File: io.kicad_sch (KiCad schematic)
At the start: 20 parts, among them J3 USB_C_Receptacle_USB2.0, J4 Conn_01x06_Male, U3 USBLC6-2SC6

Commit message: rev-7 ready
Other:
- note added: "USB ESD Protection"
- note removed: "ESD Protection"
- note removed: "Power Output"
- moved on the sheet: BUZZER1, C23, C24, C25, C26, J3, J4, LED1, R15, R16, R17, R18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

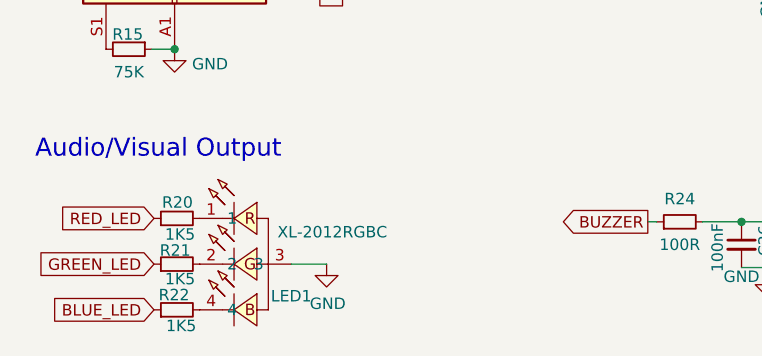
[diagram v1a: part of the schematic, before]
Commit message: fix led polarity
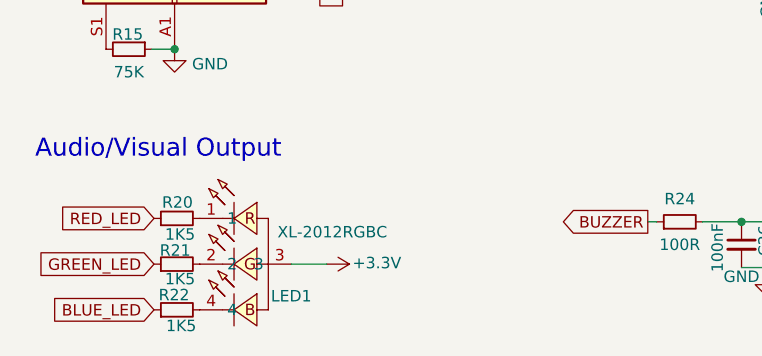
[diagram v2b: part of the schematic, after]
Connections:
- net +3.3V: now also LED1.3
- net GND: no longer LED1.3
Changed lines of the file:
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@@
     (pin "2")
-  )
-  (symbol (lib_id "power:GND") (at 44.704 79.248 0) (unit 1)
-    (in_bom yes) (on_board yes)
-    (property "Reference" "#PWR063" (id 0) (at 44.704 85.598 0)
-      (effects (font (size 1.27 1.27)) hide)
-    )
-    (property "Value" "GND" (id 1) (at 44.831 83.6422 0))
-    (property "Footprint" "" (id 2) (at 44.704 79.248 0)
-      (effects (font (size 1.27 1.27)) hide)
-    )
-    (property "Datasheet" "" (id 3) (at 44.704 79.248 0)
-      (effects (font (size 1.27 1.27)) hide)
-    )
-    (pin "1")
   )
   (symbol (lib_id "easyeda:HNB09A03") (at 96.139 74.549 180) (unit 1)
@@
     (pin "6")
   )
+  (symbol (lib_id "power:+3.3V") (at 44.704 79.248 270) (unit 1)
+    (in_bom yes) (on_board yes)
+    (property "Reference" "#PWR?" (id 0) (at 40.894 79.248 0)
+      (effects (font (size 1.27 1.27)) hide)
+    )
+    (property "Value" "+3.3V" (id 1) (at 50.292 79.121 90))
+    (property "Footprint" "" (id 2) (at 44.704 79.248 0)
+      (effects (font (size 1.27 1.27)) hide)
+    )
+    (property "Datasheet" "" (id 3) (at 44.704 79.248 0)
+      (effects (font (size 1.27 1.27)) hide)
+    )
+    (pin "1")
+  )
   (symbol (lib_id "Device:C_Small") (at 168.91 33.401 0) (unit 1)

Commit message: cleanup
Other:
- moved on the sheet: R25, U3

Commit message: kicad - 7
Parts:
- J4: footprint Connector_PinHeader_2.54mm:PinHeader_2x03_P2.54mm_Vertical -> easyeda2kicad:HDR-TH_6P-P2.54-H-M-R2-C3-S2.54

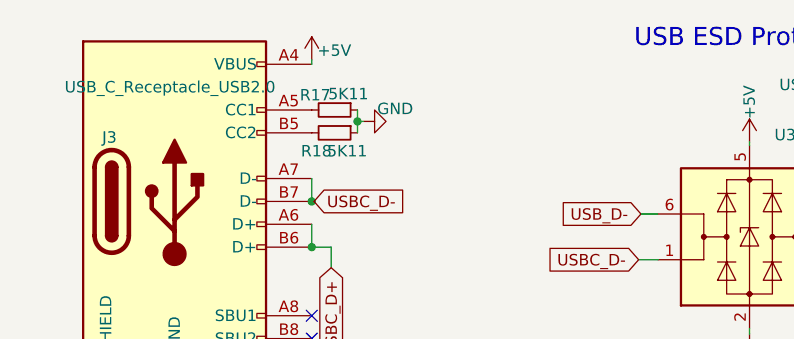
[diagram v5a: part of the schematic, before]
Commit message: migrated to kicad-7
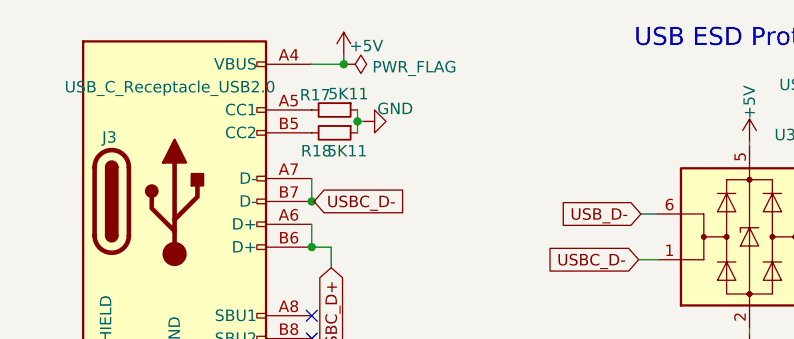
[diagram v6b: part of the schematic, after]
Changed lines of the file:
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@@
   (junction (at 43.053 37.592) (diameter 0) (color 0 0 0 0)
+  )
+  (junction (at 46.609 17.272) (diameter 0) (color 0 0 0 0)
   )
   (junction (at 48.133 23.622) (diameter 0) (color 0 0 0 0)
@@
     (stroke (width 0) (type default))
   )
+  (wire (pts (xy 46.609 17.272) (xy 43.053 17.272))
+    (stroke (width 0) (type default))
+  )
   (wire (pts (xy 135.382 31.115) (xy 136.271 31.115))
     (stroke (width 0) (type default))
@@
     (stroke (width 0) (type default))
   )
-  (wire (pts (xy 43.053 16.764) (xy 43.053 17.272))
+  (wire (pts (xy 46.609 16.256) (xy 46.609 17.272))
     (stroke (width 0) (type default))
   )
@@
     )
   )
-  (symbol (lib_id "power:+5V") (at 43.053 16.764 0) (unit 1)
-    (in_bom yes) (on_board yes) (dnp no)
-    (property "Reference" "#PWR057" (at 43.053 20.574 0)
-      (effects (font (size 1.27 1.27)) hide)
-    )
-    (property "Value" "+5V" (at 43.688 15.748 0)
+  (symbol (lib_id "power:+5V") (at 46.609 16.256 0) (unit 1)
+    (in_bom yes) (on_board yes) (dnp no)
+    (property "Reference" "#PWR057" (at 46.609 20.066 0)
+      (effects (font (size 1.27 1.27)) hide)
+    )
+    (property "Value" "+5V" (at 47.244 15.24 0)
       (effects (font (size 1.27 1.27)) (justify left))
     )
-    (property "Footprint" "" (at 43.053 16.764 0)
-      (effects (font (size 1.27 1.27)) hide)
-    )
-    (property "Datasheet" "" (at 43.053 16.764 0)
+    (property "Footprint" "" (at 46.609 16.256 0)
+      (effects (font (size 1.27 1.27)) hide)
+    )
+    (property "Datasheet" "" (at 46.609 16.256 0)
       (effects (font (size 1.27 1.27)) hide)
     )
@@
         )
       )
+    )
+  )
+  (symbol (lib_id "power:PWR_FLAG") (at 46.609 17.272 270) (unit 1)
+    (in_bom yes) (on_board yes) (dnp no) (fields_autoplaced)
+    (property "Reference" "#FLG05" (at 48.514 17.272 0)
+      (effects (font (size 1.27 1.27)) hide)
+    )
+    (property "Value" "PWR_FLAG" (at 49.784 17.5888 90)
+      (effects (font (size 1.27 1.27)) (justify left))
+    )
+    (property "Footprint" "" (at 46.609 17.272 0)
+      (effects (font (size 1.27 1.27)) hide)
+    )
+    (property "Datasheet" "~" (at 46.609 17.272 0)
+      (effects (font (size 1.27 1.27)) hide)
+    )
+    (pin "1")
+    (instances
+      (project "opilio"
+        (path "/1fd8049d-01e3-48fd-a73a-49757ed6cc50/8e36b5a2-d2db-40c0-9b7c-521fc0468cf3"
+          (reference "#FLG05") (unit 1)
+        )
+      )

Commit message: Pcb with cutouts (#4)
* cut outs design in place

* kicad 8

* updated footprints

* publish v8

* image
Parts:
- removed C26: 100nF, Capacitor_SMD:C_0402_1005Metric, symbol Device:C_Small
- added D8: B5819W, Diode_SMD:D_SOD-123, symbol Diode:MBR0530
- added Q5: CJ3134KW, easyeda2kicad:SC-70-3_L2.1-W1.3-P1.30-LS2.1-BR, symbol easyeda:CJ3134KW
- added R26: 10K, Resistor_SMD:R_0402_1005Metric, symbol Device:R_Small
- R24: value 100R -> R100; LCSC Part C106232 -> C191123
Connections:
- net +3.3V: now also R24.2
- net BUZZER: now also Q5.1 (G), R26.2; no longer R24.1
- net GND: now also Q5.2 (S), R26.1; no longer BUZZER1.2 (-)
- net at BUZZER1.1 (+): now also R24.1, D8.1 (K); no longer R24.2
- new net: BUZZER1.2 (-), D8.2 (A), Q5.3 (D)
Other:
- moved on the sheet: BUZZER1
